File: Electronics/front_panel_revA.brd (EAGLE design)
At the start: 100.3 x 111.3 mm, 0 parts

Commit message: Electronics: finished RevA
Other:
- board size 100.3 x 111.3 mm -> 100 x 94 mm

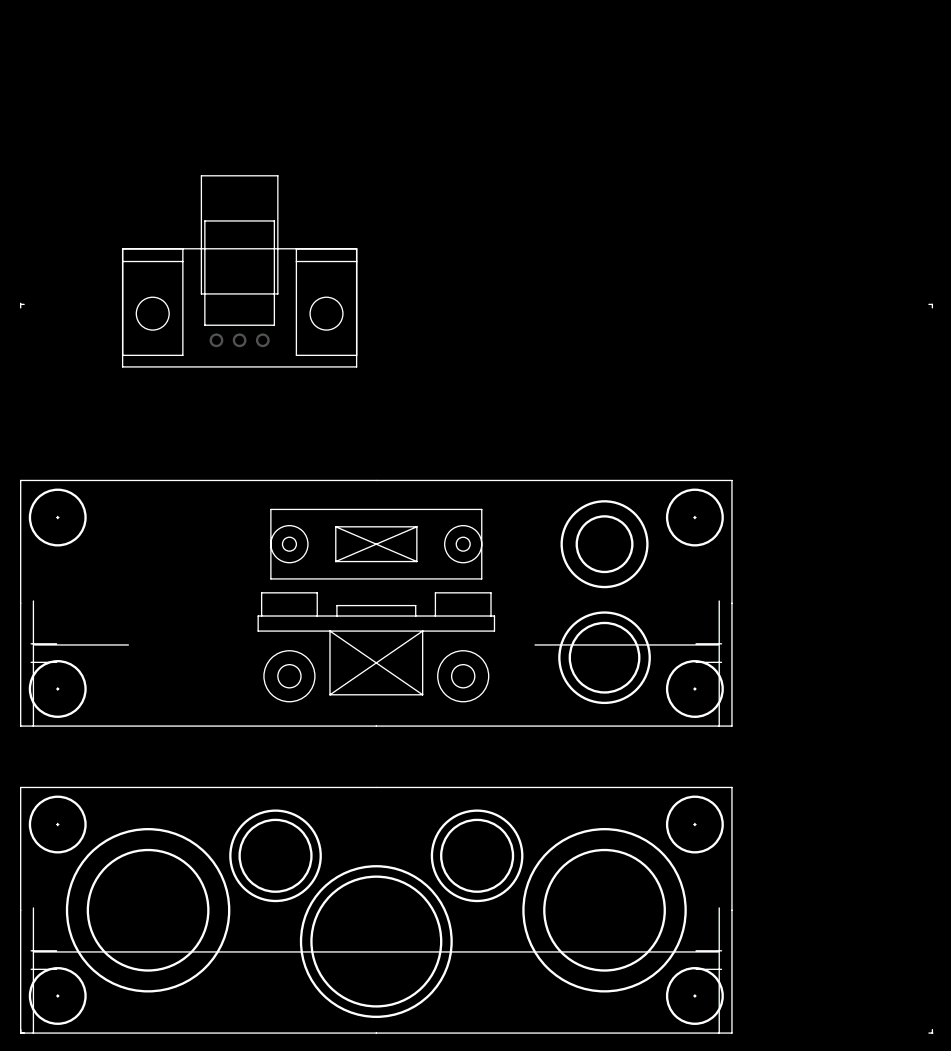
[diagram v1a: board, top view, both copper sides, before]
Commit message: Electronics: added servis connector to the back panel
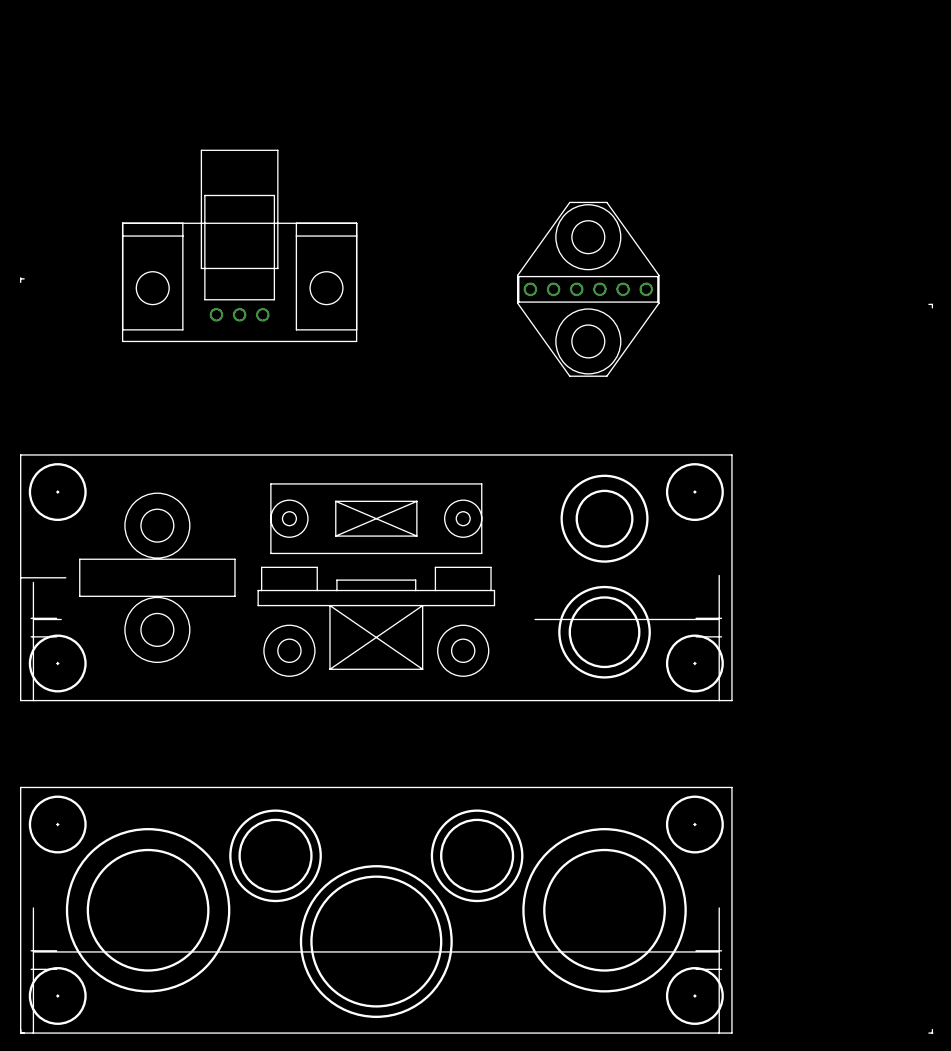
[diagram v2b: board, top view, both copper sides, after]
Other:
- board size 100 x 94 mm -> 100 x 96.8 mm
